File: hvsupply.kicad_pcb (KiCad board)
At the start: 2 copper layers, 95.2 x 165.1 mm, 53 parts, among them K1 CONN_3, K2 RELAY_2RT, P1 CONN_2, P10 CONN_1, P2 CONN_2, P3 CONN_2, P4 CONN_2, P5 CONN_1, P6 CONN_1, P7 CONN_1, P8 CONN_1, P9 CONN_1, Q1 TIP50, Q2 IRF740, Q3 IRF740, Q4 IRF740, Q5 IRF740, Q6 IRF740, SW1 SPST, U1 LR8

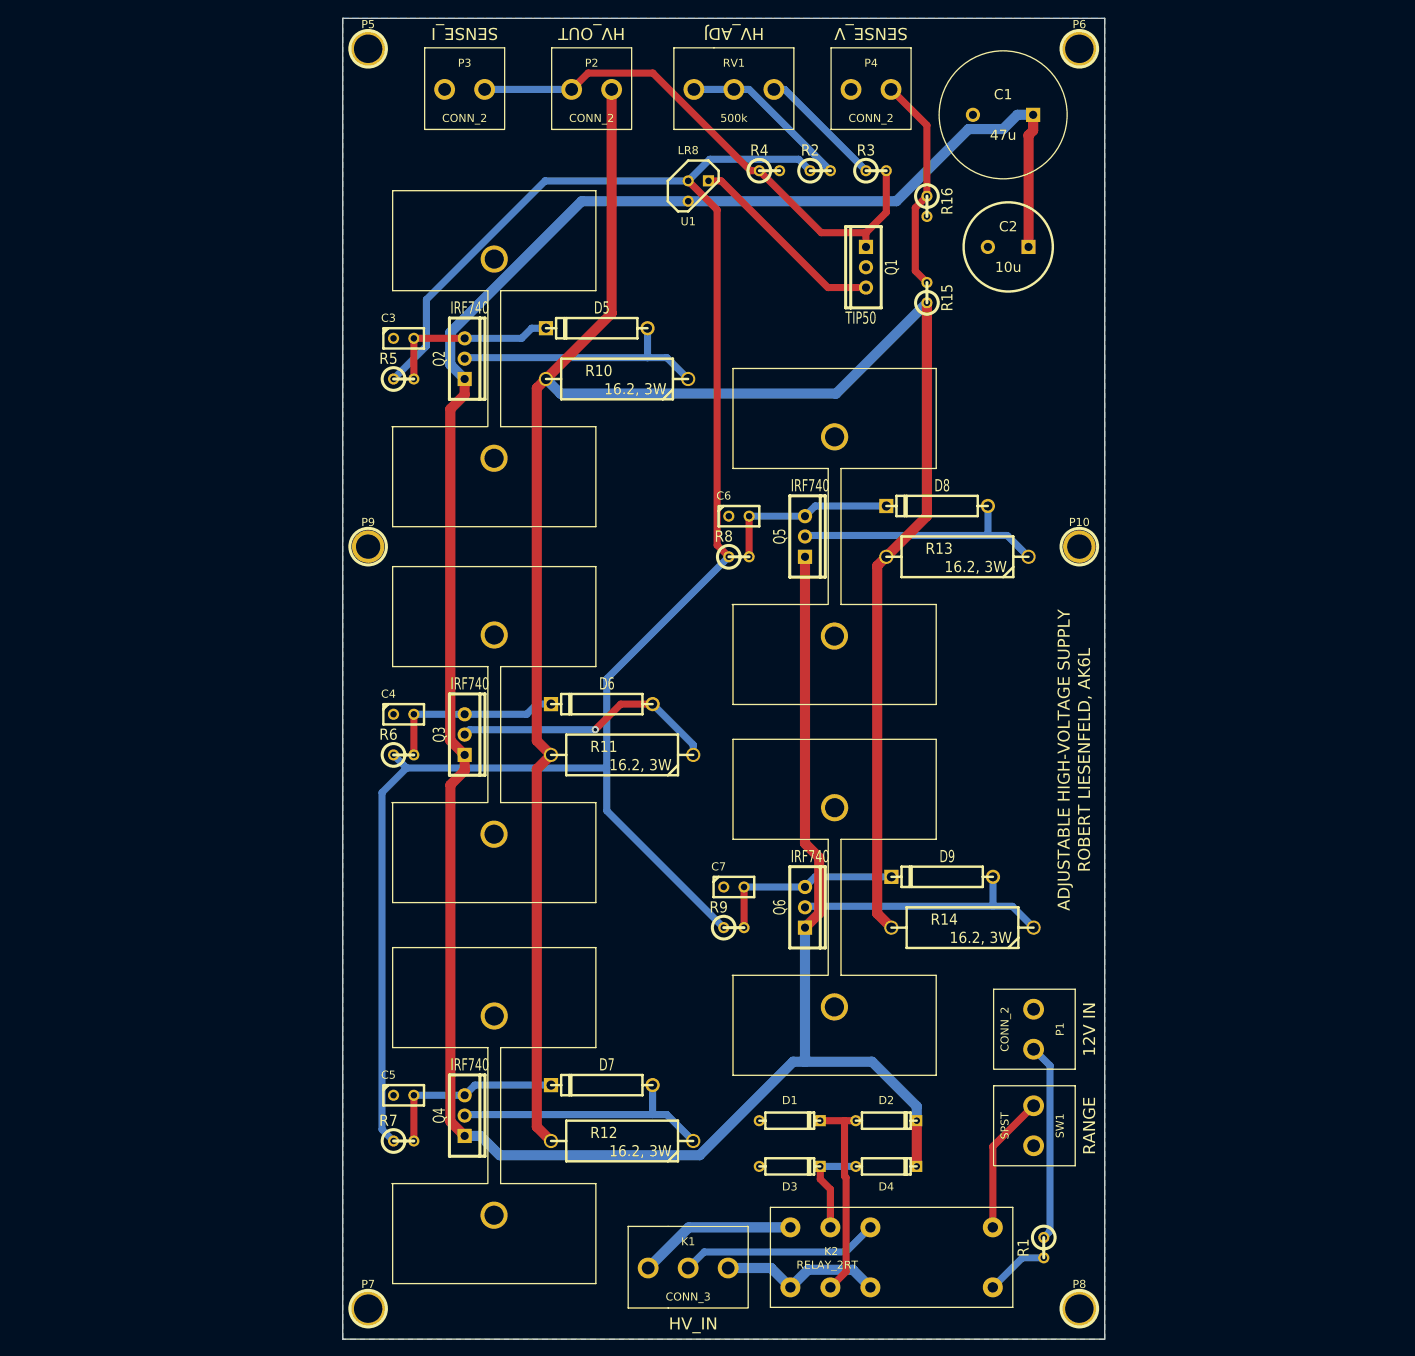
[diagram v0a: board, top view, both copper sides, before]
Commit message: Started from scratch on the PCB.  Parts placement mostly done.
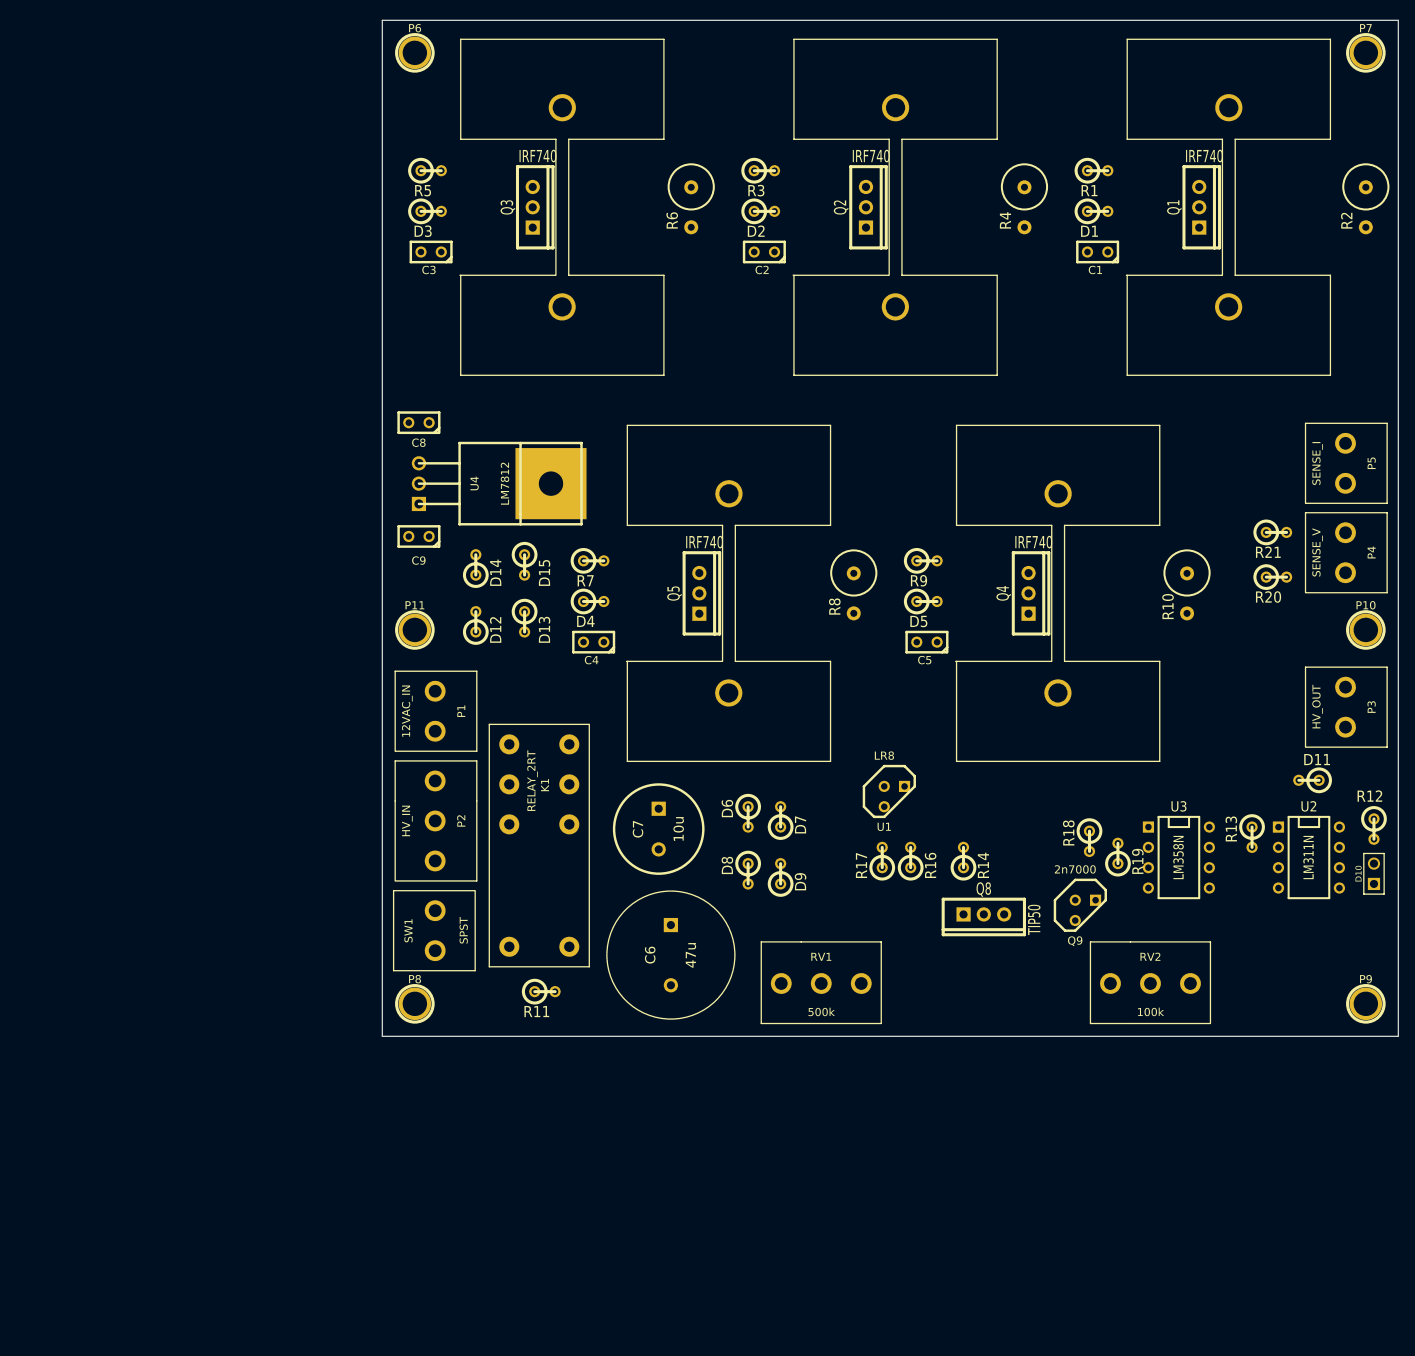
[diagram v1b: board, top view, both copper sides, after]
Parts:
- removed K2: RELAY_2RT, RTE25012
- removed Q6: IRF740, TO220_VERT_HEATSINK
- removed R15: 10M, R1
- added C8: 0.33u, C1, F.Cu at (137.2, 72.1)
- added C9: 0.1u, C1, F.Cu at (137.2, 86.4)
- added D10: LED, PIN_ARRAY_2X1, F.Cu at (256.5, 128.5)
- added D11: 1N914, R1, F.Cu at (248.4, 116.8)
- added D12: 1N4007, R1, F.Cu at (144.3, 97.0)
- added D13: 1N4007, R1, F.Cu at (150.4, 97.0)
- added D14: 1N4007, R1, F.Cu at (144.3, 89.9)
- added D15: 1N4007, R1, F.Cu at (150.4, 89.9)
- added P11: CONN_1, 1pin, F.Cu at (136.7, 98.0)
- added Q8: TIP50, TO220_VERT, F.Cu at (207.8, 133.6)
- added Q9: 2n7000, TO92-123, F.Cu at (220.5, 133.1)
- added R17: 2.2k, R1, F.Cu at (195.1, 126.5)
- added R18: 10k, R1, F.Cu at (221.0, 124.5)
- added R19: 10k, R1, F.Cu at (224.5, 126.0)
- added R20: 10M, R1, F.Cu at (244.3, 91.4)
- added R21: 10k, R1, F.Cu at (244.3, 85.9)
- added RV2: 100k, RJ128-5.0-3, F.Cu at (228.6, 142.2)
- added U2: LM311N, DIP-8__300, F.Cu at (248.4, 126.5)
- added U3: LM358N, DIP-8__300, F.Cu at (232.2, 126.5)
- added U4: LM7812, TO220, F.Cu at (137.2, 79.8)
- C1: value 47u -> .01; footprint CP7P5X16 -> C1
- C2: value 10u -> .01; footprint C2V10 -> C1
- C6: value .01 -> 47u; footprint C1 -> CP7P5X16
- C7: value .01 -> 10u; footprint C1 -> C2V10
- D1, D2, D3, D4: value 1N4007 -> 16V, 1.3W; footprint D3 -> R1
- D5: footprint D5 -> R1
- D6, D7, D8, D9: value 16V, 1.3W -> 1N4007; footprint D5 -> R1
- K1: value CONN_3 -> RELAY_2RT; footprint RJ128-5.0-3 -> RTE25012
- P1: value CONN_2 -> 12VAC_IN
- P2: value CONN_2 -> HV_IN; footprint RJ128-5.0-2 -> RJ128-5.0-3
- P3: value CONN_2 -> HV_OUT
- P4: value CONN_2 -> SENSE_V
- P5: value CONN_1 -> SENSE_I; footprint 1pin -> RJ128-5.0-2
- Q1: value TIP50 -> IRF740; footprint TO220_VERT -> TO220_VERT_HEATSINK
- R1: value 330 -> 100
- R10: footprint R7 -> RS02B16R20FE70
- R11: value 16.2, 3W -> 330; footprint R7 -> R1
- R12: value 16.2, 3W -> 220; footprint R7 -> R1
- R13: value 16.2, 3W -> 3.3k; footprint R7 -> R1
- R14: value 16.2, 3W -> 100; footprint R7 -> R1
- R16: value 10k -> 2.2k
- R2: value 2.2k -> 16.2, 3W; footprint R1 -> RS02B16R20FE70
- R3: value 2.2k -> 100
- R4: value 2.37 -> 16.2, 3W; footprint R1 -> RS02B16R20FE70
- R6, R8: value 100 -> 16.2, 3W; footprint R1 -> RS02B16R20FE70
- moved P7 200.5 mm to (255.5, 25.9)
- moved P9 137.2 mm to (255.5, 144.8)
- moved R1 134.8 mm to (222.0, 40.6), turned to 0 degrees
- moved P3 134.5 mm to (253.0, 107.7), turned to 90 degrees
- moved P5 132.7 mm to (253.0, 77.2), turned to 90 degrees
- moved D3 127.5 mm to (138.7, 45.7)
- moved D1 120.0 mm to (222.0, 45.7)
- moved D2 114.7 mm to (180.3, 45.7)
- moved RV1 112.3 mm to (187.5, 142.2)
- moved R12 101.7 mm to (256.5, 122.9), turned to 270 degrees
- moved Q4 96.1 mm to (213.4, 93.5)
- moved P2 93.5 mm to (139.2, 121.9), turned to 90 degrees
- moved P8 91.4 mm to (136.7, 144.8)
- moved C5 86.5 mm to (200.7, 99.6), turned to 180 degrees
- moved P1 84.7 mm to (139.2, 108.2)
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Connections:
- C1 pad 1: /HV_UNREG -> GND
- C1 pad 2: GND -> N-000001
- C2 pad 1: /HV_UNREG -> GND
- C2 pad 2: GND -> N-000002
- C3 pad 2: N-000006 -> N-0000010
- C4 pad 2: N-000007 -> N-000009
- C5 pad 2: N-000009 -> N-000007
- C6 pad 1: GND -> /HV_UNREG
- C6 pad 2: N-0000012 -> GND
- C7 pad 1: GND -> /HV_UNREG
- C7 pad 2: N-0000010 -> GND
- D1 pad 1: GND -> N-0000016
- D1 pad 2: N-0000011 -> N-000001
- D2 pad 1: N-0000011 -> N-0000015
- D2 pad 2: /HV_UNREG -> N-000002
- D3 pad 1: GND -> N-0000011
- D3 pad 2: N-0000023 -> N-0000010
- D4 pad 1: N-0000023 -> N-000008
- D4 pad 2: /HV_UNREG -> N-000009
- D5 pad 1: N-000005 -> N-000006
- D5 pad 2: N-000006 -> N-000007
- D6 pad 1: N-000008 -> GND
- D6 pad 2: N-000007 -> N-0000012
- D7 pad 1: N-0000013 -> N-0000012
- D7 pad 2: N-000009 -> /HV_UNREG
- D8 pad 1: N-0000016 -> GND
- D8 pad 2: N-0000012 -> N-0000033
- D9 pad 1: N-0000015 -> N-0000033
- D9 pad 2: N-0000010 -> /HV_UNREG
- K1 pad 1: /HV_IN_HI -> /HV_IN_LO
- K1 pad 3: /HV_IN_LO -> N-0000014
- P1 pad 1: /12V_IN -> /12VAC_IN
- P1 pad 2: GND -> N-0000023
- P2 pad 1: /HV_OUT -> /HV_IN_HI
- P2 pad 2: /SENSE_I -> N-0000014
- P3 pad 1: /SENSE_I -> /HV_OUT
- P3 pad 2: GND -> N-0000027
- P5 pad 1: GND -> /SENSE_I
- Q1 pad 1: /SENSE_I -> /HV_UNREG
- Q1 pad 2: N-000004 -> N-000001
- Q1 pad 3: GND -> N-0000016
- Q2 pad 2: N-000006 -> N-000002
- Q2 pad 3: N-000005 -> N-0000015
- Q3 pad 2: N-000007 -> N-0000010
- Q3 pad 3: N-000008 -> N-0000011
- Q4 pad 3: N-0000013 -> N-000008
- Q5 pad 2: N-0000012 -> N-000007
- Q5 pad 3: N-0000016 -> N-000006
- R1 pad 1: /12V_IN -> N-0000032
- R1 pad 2: N-000002 -> N-000001
- R10 pad 1: N-000005 -> N-000006
- R11 pad 1: N-000008 -> N-0000021
- R11 pad 2: /HV_OUT -> GND
- R12 pad 1: N-0000013 -> +12V
- R12 pad 2: /HV_OUT -> N-000003
- R13 pad 1: N-0000016 -> +12V
- R13 pad 2: /HV_OUT -> N-0000025
- R14 pad 1: N-0000015 -> N-0000017
- R14 pad 2: /HV_OUT -> N-0000026
- R16 pad 1: /SENSE_V -> N-0000032
- R16 pad 2: GND -> N-0000030
- R2 pad 1: N-0000025 -> N-0000016
- R2 pad 2: N-0000022 -> /HV_OUT
- R3 pad 1: N-0000024 -> N-0000032
- R3 pad 2: /SENSE_I -> N-000002
- R4 pad 1: /SENSE_I -> N-0000015
- R4 pad 2: GND -> /HV_OUT
- R5 pad 1: N-0000025 -> N-0000032
- R5 pad 2: N-000006 -> N-0000010
- R6 pad 1: N-0000025 -> N-0000011
- R6 pad 2: N-000007 -> /HV_OUT
- R7 pad 1: N-0000025 -> N-0000032
- R8 pad 1: N-0000025 -> N-000008
- R8 pad 2: N-0000012 -> /HV_OUT
- R9 pad 1: N-0000025 -> N-0000032
- R9 pad 2: N-0000010 -> N-000007
- RV1 pad 1: N-0000024 -> N-0000031
- RV1 pad 2: N-0000022 -> N-0000030
- RV1 pad 3: N-0000022 -> N-0000030
- SW1 pad 1: GND -> N-000004
- SW1 pad 2: N-0000017 -> N-0000021
- U1 pad 2: N-0000025 -> N-0000032
- U1 pad 3: N-000004 -> N-0000030
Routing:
- net /HV_UNREG: track 341.7 -> 0.00 mm
- net /HV_OUT: track 272.0 -> 0.00 mm
- net N-0000025: track 251.1 -> 0.00 mm
- net /SENSE_I: track 67.4 -> 0.00 mm
- net N-0000013: track 33.7 -> 0.00 mm
- net N-000008: track 33.5 -> 0.00 mm, vias 1 -> 0
- net N-0000015: track 33.4 -> 0.00 mm
- net N-0000016: track 32.8 -> 0.00 mm
- net N-000005: track 32.8 -> 0.00 mm
- net /SENSE_V: track 27.2 -> 0.00 mm
- net N-0000011: track 26.2 -> 0.00 mm
- net N-000004: track 25.2 -> 0.00 mm
- net N-0000014: track 24.9 -> 0.00 mm
- net /12V_IN: track 24.7 -> 0.00 mm
- net N-0000010: track 24.0 -> 0.00 mm
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- removed copper zone on B.Cu, net GND
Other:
- board size 95.2 x 165.1 mm -> 127 x 127 mm
- net class Default: trace_width 0.889 -> 0.254
- net class Power Rail removed
- rule pad_to_mask_clearance: 0.00254 -> 0.2
- board text removed: "12V IN"
- board text removed: "ADJUSTABLE HIGH-VOLTAGE SUPPLY"
- board text removed: "HV_ADJ"
- board text removed: "HV_IN"
- board text removed: "HV_OUT"
- board text removed: "RANGE"
- board text removed: "ROBERT LIESENFELD, AK6L"
- board text removed: "SENSE_I"
- board text removed: "SENSE_V"

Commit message: Most traces run. 12V supply section remains.
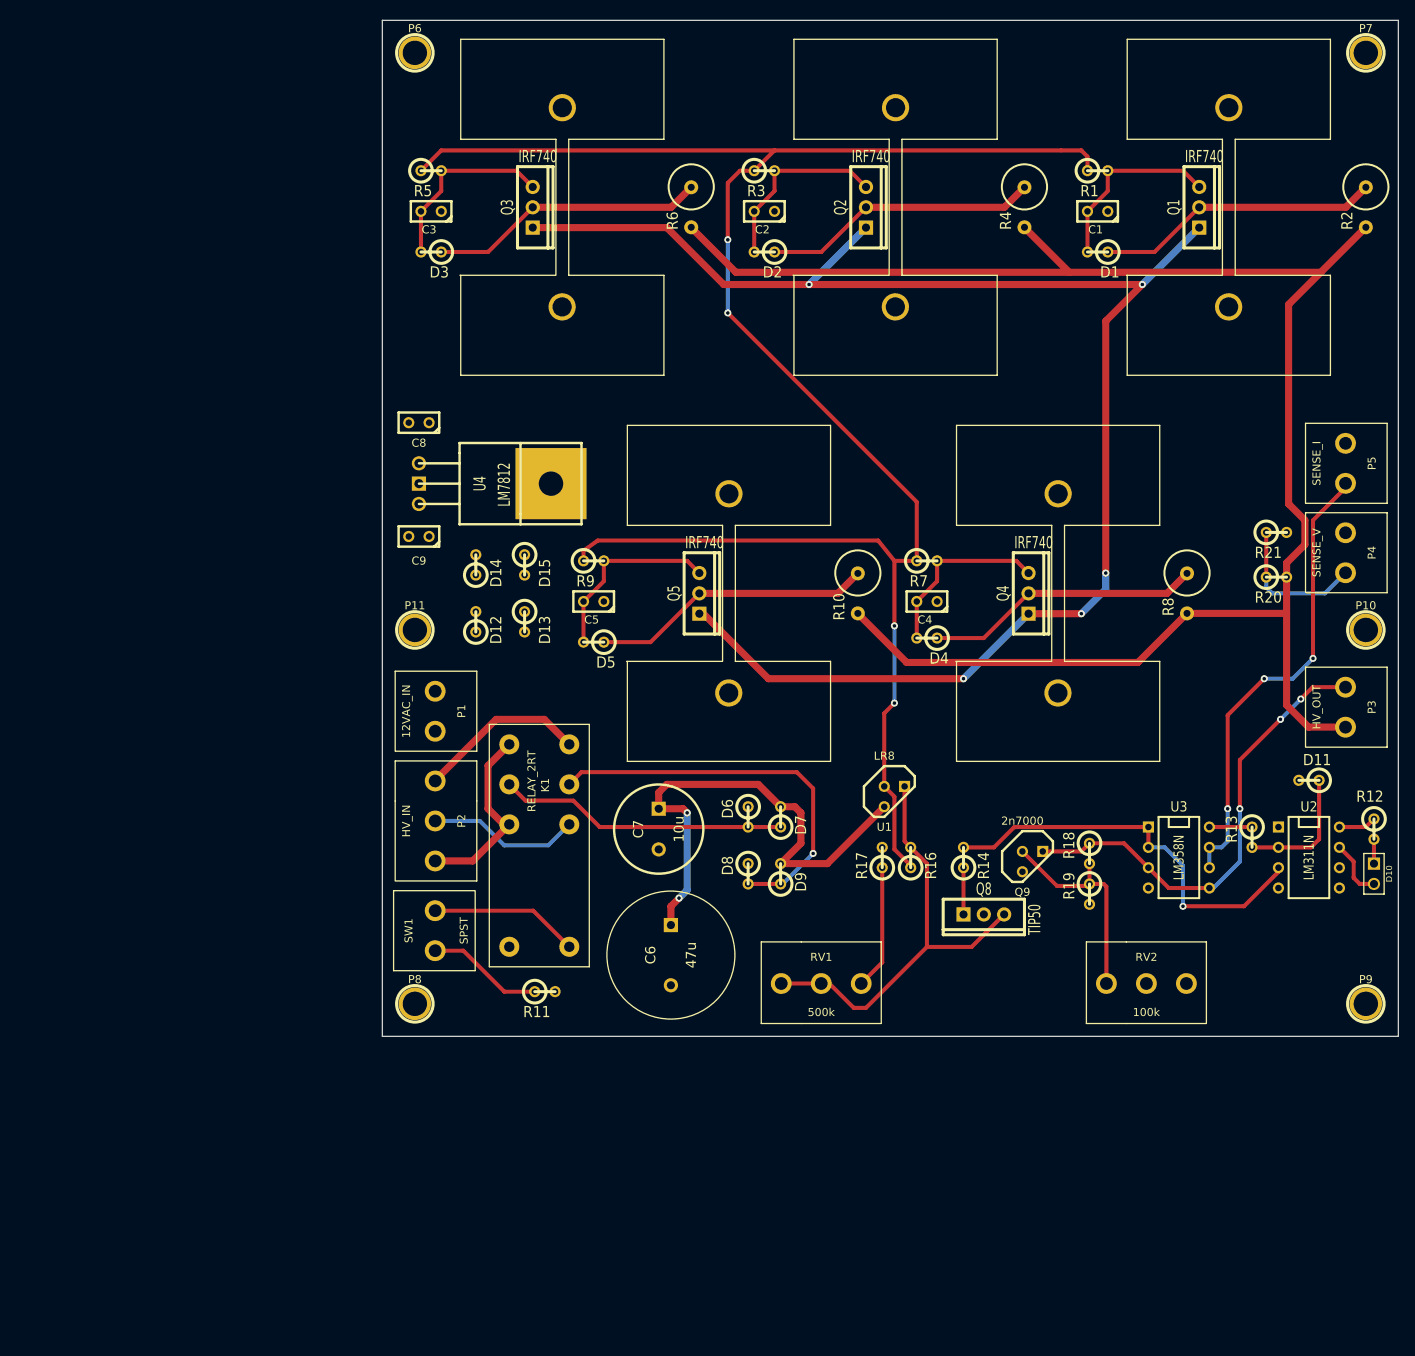
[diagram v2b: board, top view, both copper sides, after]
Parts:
- Q9: footprint TO92-123 -> TO92DGS
- U4: footprint TO220 -> LM78XX
- moved C4 42.0 mm to (200.7, 94.5)
- moved C5 42.0 mm to (159.0, 94.5)
- moved D5 42.0 mm to (159.0, 99.6), turned to 180 degrees
- moved D4 41.9 mm to (200.7, 99.1), turned to 180 degrees
- moved R7 41.7 mm to (200.7, 89.4)
- moved R8 41.7 mm to (233.2, 93.5)
- moved R9 41.7 mm to (159.0, 89.4)
- moved R10 41.1 mm to (192.0, 93.5)
- moved Q9 8.99 mm to (213.9, 127.0)
- moved R19 6.20 mm to (221.0, 131.1), turned to 270 degrees
- moved C1 5.08 mm to (222.0, 45.7)
- moved C2 5.08 mm to (180.3, 45.7)
- moved C3 5.08 mm to (138.7, 45.7)
- moved D1 5.08 mm to (222.0, 50.8), turned to 180 degrees
- moved D2 5.08 mm to (180.3, 50.8), turned to 180 degrees
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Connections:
- P3 pad 2: N-0000027 -> N-0000028
- R17 pad 2: N-0000027 -> N-0000028
- R18 pad 1: N-0000027 -> N-0000028
- R18 pad 2: N-000005 (its old number) -> N-0000020
- R19 pad 1: N-000005 (its old number) -> N-0000020
- RV2 pad 3: N-000005 (its old number) -> N-0000020
- U3 pad 3: N-0000027 -> N-0000028
- U3 pad 5: N-0000027 -> N-0000028
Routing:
- net /HV_UNREG: track 0.00 -> 261.7 mm, vias 0 -> 7
- net N-0000032: track 0.00 -> 235.8 mm, vias 0 -> 4
- net /HV_OUT: track 0.00 -> 221.7 mm
- net N-0000028: track 0.00 -> 58.4 mm, vias 0 -> 3
- net /SENSE_I: track 0.00 -> 58.1 mm, vias 0 -> 3
- net N-0000030: track 0.00 -> 55.2 mm
- net N-0000025: track 0.00 -> 51.3 mm, vias 0 -> 1
- net N-0000033: track 0.00 -> 49.8 mm, vias 0 -> 1
- net N-0000011: track 0.00 -> 36.1 mm
- net N-0000015: track 0.00 -> 35.6 mm
- net N-000005: track 0.00 -> 35.3 mm
- net N-000007: track 0.00 -> 34.6 mm
- net N-0000014: track 0.00 -> 34.6 mm
- net N-0000010: track 0.00 -> 34.6 mm
- net N-0000020: track 0.00 -> 27.2 mm
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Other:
- net class Default: trace_width 0.254 -> 0.508
- net class HV added: clearance 0.254, trace_width 0.889, via_dia 0.889, via_drill 0.635

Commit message: Generated new drill files.
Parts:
- moved R20 48.7 mm to (197.6, 105.2), turned to 270 degrees
- moved Q4 47.5 mm to (167.6, 106.2)
- moved R21 47.5 mm to (198.6, 98.6)
- moved D10 47.5 mm to (210.8, 141.2)
- moved D7 47.5 mm to (136.7, 134.1)
- moved D9 47.5 mm to (136.7, 141.2)
- moved R12 47.5 mm to (210.8, 135.6)
- moved P1 47.5 mm to (93.5, 120.9)
- moved P2 47.5 mm to (93.5, 134.6)
- moved SW1 47.5 mm to (93.5, 148.3)
- moved C1 47.5 mm to (176.3, 58.4)
- moved C2 47.5 mm to (134.6, 58.4)
- moved C3 47.5 mm to (93.0, 58.4)
- moved C4 47.5 mm to (154.9, 107.2)
- moved C6 47.5 mm to (122.9, 151.4)
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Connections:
- U4 pad GND: (no net) -> GND
- U4 pad VI: (no net) -> N-0000019
- U4 pad VO: (no net) -> +12V
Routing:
- net +12V: track 10.1 -> 215.5 mm, vias 0 -> 6
- net N-0000019: track 0.00 -> 35.8 mm
- net N-0000023: track 0.00 -> 26.6 mm
- net /12VAC_IN: track 0.00 -> 23.9 mm
- net N-0000028: track 58.4 -> 80.2 mm
- net /HV_UNREG: track 261.7 -> 278.0 mm
- net /SENSE_V: track 18.1 -> 15.2 mm
- net N-0000030: track 55.2 -> 52.7 mm, vias 0 -> 2
- net /HV_OUT: track 221.7 -> 223.7 mm
- added copper zone on B.Cu, net GND
- added copper zone on F.Cu, net GND
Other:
- board text added: "High-Voltage Adjustable Bench Supply"
- board text added: "Robert Liesenfeld AK6L"

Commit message: Had to put something on the back silkscreen.
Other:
- board text added: "xunil@xunil.net"
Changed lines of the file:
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@@
     (area 86.792999 34.468999 213.943001 161.619001)
     (thickness 1.6)
-    (drawings 6)
+    (drawings 7)
     (tracks 313)
     (zones 0)
@@
     (visible_elements FFFFE77F)
     (pcbplotparams
-      (layerselection 3178497)
-      (usegerberextensions false)
+      (layerselection 1048576)
+      (usegerberextensions true)
       (excludeedgelayer true)
       (linewidth 0.100000)
@@
       (padsonsilk false)
       (subtractmaskfromsilk false)
-      (outputformat 5)
+      (outputformat 1)
       (mirror false)
       (drillshape 0)
       (scaleselection 1)
-      (outputdirectory ""))
+      (outputdirectory gerbers/))
   )
   (net 0 "")
@@
     )
   )
+  (gr_text xunil@xunil.net (at 192.024 82.804) (layer B.SilkS)
+    (effects (font (size 1.5 1.5) (thickness 0.3)) (justify mirror))
+  )
   (gr_text "Robert Liesenfeld AK6L" (at 158.496 82.296) (layer F.SilkS)

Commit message: Fixed anchor spacing for heatsinks, drill diameter for balance resistors.
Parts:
- moved Q3 0.13 mm to (105.6, 57.8)
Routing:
- net N-0000032: track 235.8 -> 235.4 mm, vias 4 -> 2
